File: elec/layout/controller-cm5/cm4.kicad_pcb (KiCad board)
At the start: 4 copper layers, 10 parts

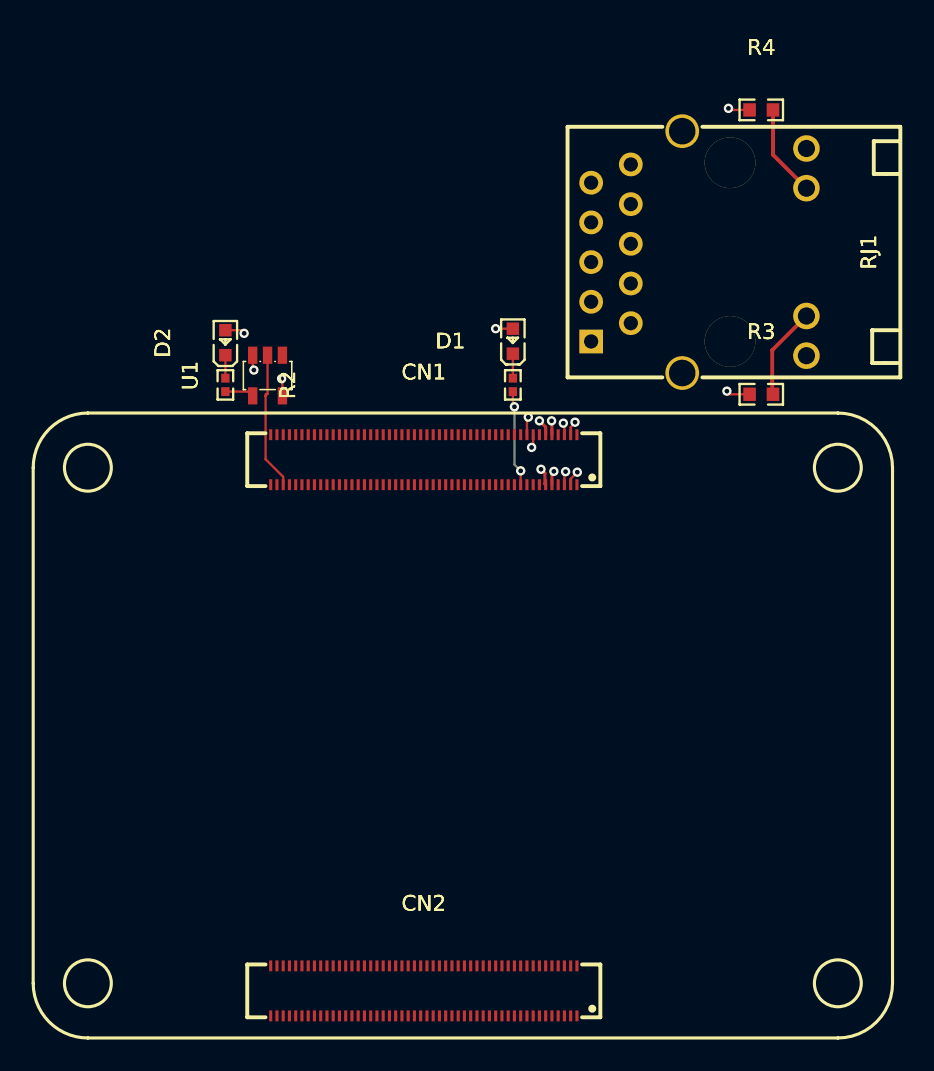
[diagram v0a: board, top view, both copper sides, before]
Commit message: re-sync layout + place mounting holes
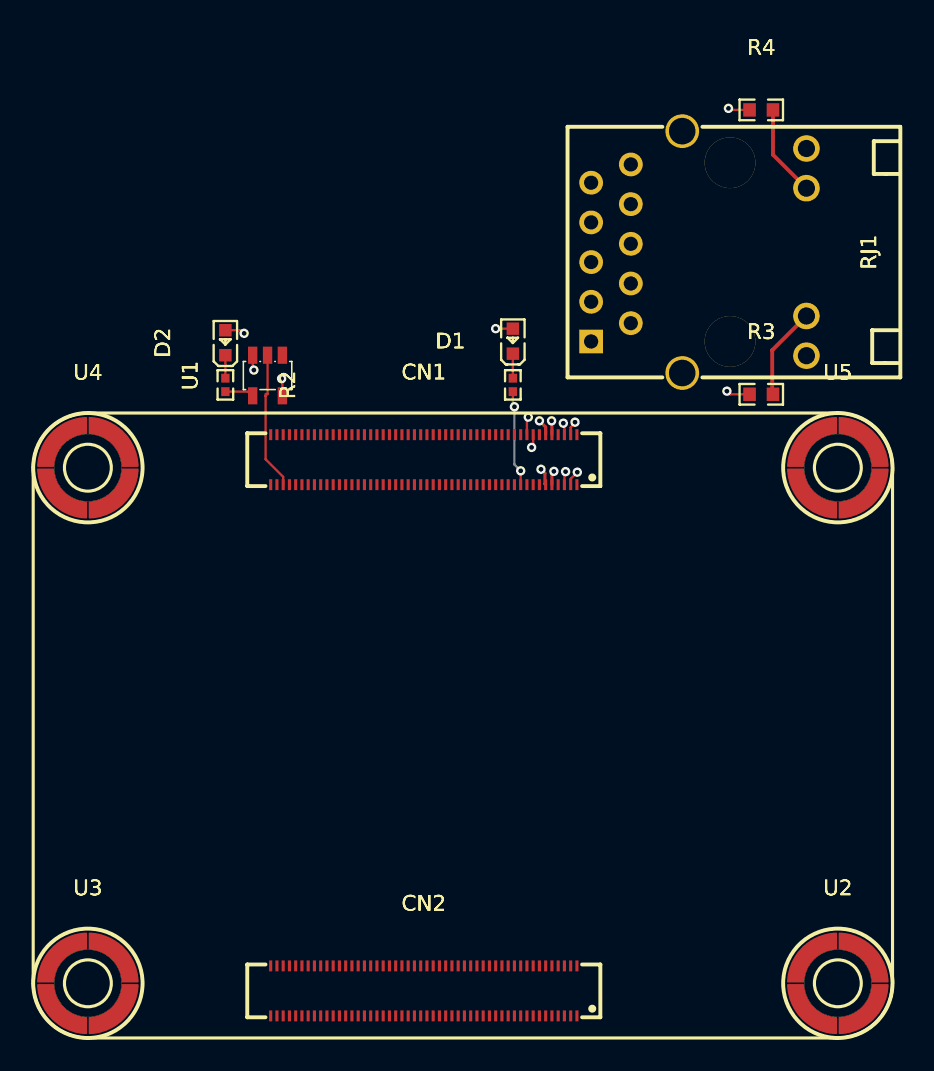
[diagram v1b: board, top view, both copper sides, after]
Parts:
- added U2: , atopile:SMD_BD5.6-D4.1-12eb58, F.Cu at (176.4, 136.8)
- added U3: , atopile:SMD_BD5.6-D4.1-12eb58, F.Cu at (128.4, 136.8)
- added U4: , atopile:SMD_BD5.6-D4.1-12eb58, F.Cu at (128.4, 103.8)
- added U5: , atopile:SMD_BD5.6-D4.1-12eb58, F.Cu at (176.4, 103.8)
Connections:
- net cm4-cathode renamed cm5-cathode
- net cm4-cathode-1 renamed cm5-cathode-1
- net cm4-line renamed cm5-line-3
- net cm4-line-1 renamed pins[57]
- net cm4-line-2 renamed cm5-line-7
- net cm4-line-3 renamed cm5-line-6
- net cm4-line-4 renamed pins[45]
- net cm4-line-5 renamed Y
- net cm4-line-6 renamed cm5-line-2
- net cm4-line-7 renamed cm5-line-1
- net cm4-pins[23] renamed cm5-line
- net cm4-pins[28] renamed cm5-line-10
- net cm4-pins[40] renamed cm5-pins[40]
- net cm4-pins[44] renamed cm5-pins[44]
- net cm4-pins[44]-1 renamed cm5-pins[44]-1
- net cm4-pins[98] renamed cm5-pins[98]
- net cm4-pins[99] renamed cm5-pins[99]
- net cm4.hdi_a-pins[15] renamed cm5.hdi_a-pins[15]
- net cm4.hdi_a-pins[17] renamed cm5.hdi_a-pins[17]
- net cm4.hdi_a-pins[34] renamed cm5.hdi_a-pins[34]
- net cm4.hdi_a-pins[35] renamed cm5.hdi_a-pins[35]
- net cm4.hdi_a-pins[56] renamed cm5.hdi_a-pins[56]
- net cm4.hdi_a-pins[62] renamed cm5.hdi_a-pins[62]
- net cm4.hdi_a-pins[68] renamed cm5.hdi_a-pins[68]
- net cm4.hdi_a-pins[74] renamed cm5.hdi_a-pins[74]
- net cm4.hdi_a-pins[88] renamed cm5.hdi_a-pins[88]
- net cm4.hdi_a-pins[92] renamed cm5.hdi_a-pins[92]
- net cm4.hdi_a-pins[93] renamed cm5.hdi_a-pins[93]
- net cm4.hdi_a-pins[94] renamed cm5.hdi_a-pins[94]
- net cm4.hdi_a-pins[98] renamed cm5.hdi_a-pins[98]
- net cm4.hdi_a-pins[99] renamed cm5.hdi_a-pins[99]
- net cm4.hdi_b-pins[15] renamed cm5.hdi_b-pins[15]
- net cm4.hdi_b-pins[17] renamed cm5.hdi_b-pins[17]
- net cm4.hdi_b-pins[23] renamed pins[23]
- net cm4.hdi_b-pins[28] renamed pins[28]
- net cm4.hdi_b-pins[34] renamed cm5.hdi_b-pins[34]
- net cm4.hdi_b-pins[35] renamed cm5-pins[35]
- net cm4.hdi_b-pins[40] renamed cm5.hdi_b-pins[40]
- net cm4.hdi_b-pins[56] renamed cm5-pins[56]
- net cm4.hdi_b-pins[62] renamed cm5-pins[62]
- net cm4.hdi_b-pins[68] renamed cm5-pins[68]
- net cm4.hdi_b-pins[74] renamed cm5.hdi_b-pins[74]
- net cm4.hdi_b-pins[88] renamed cm5.hdi_b-pins[88]
- net cm4.hdi_b-pins[92] renamed cm5.hdi_b-pins[92]
- net cm4.hdi_b-pins[93] renamed cm5.hdi_b-pins[93]
- net cm4.hdi_b-pins[94] renamed cm5.hdi_b-pins[94]
- net pins[30] renamed cm5-line-8
- net pins[43] renamed cm5-line-4
- net pins[47] renamed cm5-line-5
- net pins[50] renamed cm5-line-9
- CN1 pad 15: line -> line-1
- CN1 pad 17: line-1 -> line
- CN1 pad 27: line-2 -> line-3
- CN1 pad 82: line-3 -> line-2
- R3 pad 2: rj45-anode -> rj45-anode-1
- R4 pad 2: rj45-anode-1 -> rj45-anode
- RJ1 pad 12: rj45-anode -> rj45-anode-1
- RJ1 pad 13: rj45-anode-1 -> rj45-anode

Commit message: map i2c connections
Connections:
- net pins[49] renamed cm5.hdi_b-pins[49]
- CN1 pad 12: cm5-line -> cm5-line-2
- CN1 pad 15: line-1 -> line-2
- CN1 pad 17: line -> line-1
- CN1 pad 19: cm5-line-6 -> pins[37]
- CN1 pad 20: SCL -> cm5-line-9
- CN1 pad 24: cm5-line-5 -> cm5-line-8
- CN1 pad 25: cm5-line-2 -> cm5-pins[49]
- CN1 pad 28: cm5-line-3 -> SCL
- CN1 pad 29: pins[57] -> SDA
- CN1 pad 75: cm5-line-9 -> cm5-line-5
- CN1 pad 77: cm5-line-1 -> cm5-line
- CN1 pad 78: cm5-pins[44]-1 -> cm5-pins[44]
- CN1 pad 81: SDA -> cm5-line-6
- CN1 pad 82: line-2 -> line
- CN1 pad 85: cm5-line-8 -> cm5-line-1
- CN1 pad 86: cm5-line-10 -> cm5-line-3
- CN2 pad 78: cm5-pins[44] -> cm5-pins[44]-1
- D1 pad 1: cm5-cathode-1 -> cm5-cathode
- D2 pad 1: cm5-cathode -> cm5-cathode-1
- R1 pad 1: cm5-cathode-1 -> cm5-cathode
- R2 pad 1: cm5-cathode -> cm5-cathode-1
- R3 pad 2: rj45-anode-1 -> rj45-anode
- R4 pad 2: rj45-anode -> rj45-anode-1
- RJ1 pad 12: rj45-anode-1 -> rj45-anode
- RJ1 pad 13: rj45-anode -> rj45-anode-1
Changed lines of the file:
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@@
 	(net 0 "")
 	(net 1 "pins[20]")
-	(net 2 "cm5-pins[44]-1")
+	(net 2 "cm5-pins[44]")
 	(net 3 "cm5-pins[62]")
 	(net 4 "cm5.hdi_a-pins[74]")
 	(net 5 "cm5-line-4")
-	(net 6 "cm5-line-5")
+	(net 6 "cm5-line-8")
 	(net 7 "cm5.hdi_b-pins[74]")
 	(net 8 "cm5.hdi_a-pins[62]")
@@
 	(net 11 "pins[46]")
 	(net 12 "pins[67]")
-	(net 13 "cm5-line-10")
+	(net 13 "cm5-line-3")
 	(net 14 "UART_TX")
 	(net 15 "pins[5]")
 	(net 16 "VCC_5V")
 	(net 17 "UART_RX")
-	(net 18 "cm5-line-3")
+	(net 18 "SCL")
 	(net 19 "HDMI0_D1_N")
 	(net 20 "HDMI0_D2_N")
@@
 	(net 28 "pins[90]")
 	(net 29 "pins[82]")
-	(net 30 "line-1")
+	(net 30 "line-2")
 	(net 31 "pins[58]")
-	(net 32 "pins[57]")
+	(net 32 "SDA")
 	(net 33 "HDMI0_D0_P")
-	(net 34 "cm5-pins[44]")
+	(net 34 "cm5-pins[44]-1")
 	(net 35 "pins[76]")
 	(net 36 "cm5.hdi_a-pins[88]")
 	(net 37 "HDMI1_D2_P")
-	(net 38 "line-2")
+	(net 38 "line")
 	(net 39 "HDMI1_CK_N")
 	(net 40 "pins[79]")
@@
 	(net 46 "pins[33]")
 	(net 47 "pins[66]")
-	(net 48 "cm5-line-9")
+	(net 48 "cm5-line-5")
 	(net 49 "cm5.hdi_b-pins[88]")
 	(net 50 "cm5.hdi_b-pins[92]")
-	(net 51 "cm5-line-6")
-	(net 52 "cm5-line")
+	(net 51 "pins[37]")
+	(net 52 "cm5-line-2")
 	(net 53 "pins[29]")
-	(net 54 "pins[49]")
+	(net 54 "cm5.hdi_b-pins[49]")
 	(net 55 "HDMI1_D0_N")
 	(net 56 "cm5-pins[35]")
@@
 	(net 67 "rj45.connector-net-1")
 	(net 68 "Y")
-	(net 69 "cm5-cathode-1")
-	(net 70 "cm5-cathode")
-	(net 71 "rj45-anode")
+	(net 69 "cm5-cathode")
+	(net 70 "cm5-cathode-1")
+	(net 71 "rj45-anode-1")
 	(net 72 "rj45.connector-net")
 	(net 73 "N_C_")
-	(net 74 "rj45-anode-1")
+	(net 74 "rj45-anode")
 	(net 75 "pins[45]")
 	(net 76 "pins[3]")
@@
 	(net 82 "pins[41]")
 	(net 83 "pins[70]")
-	(net 84 "cm5-line-2")
+	(net 84 "cm5-pins[49]")
 	(net 85 "cm5.hdi_a-pins[98]")
 	(net 86 "cm5.hdi_b-pins[34]")
@@
 	(net 92 "cm5.hdi_b-pins[40]")
 	(net 93 "pins[91]")
-	(net 94 "SCL")
+	(net 94 "cm5-line-9")
 	(net 95 "pins[64]")
 	(net 96 "pins[9]")
@@
 	(net 115 "pins[72]")
 	(net 116 "HDMI0_CK_N")
-	(net 117 "cm5-line-8")
+	(net 117 "cm5-line-1")
 	(net 118 "HDMI0_D2_P")
 	(net 119 "pins[22]")
-	(net 120 "line")
+	(net 120 "line-1")
 	(net 121 "pins[80]")
 	(net 122 "cm5.hdi_b-pins[94]")
@@
 	(net 124 "pins[96]")
 	(net 125 "pins[14]")
-	(net 126 "cm5-line-1")
+	(net 126 "cm5-line")
 	(net 127 "cm5.hdi_a-pins[94]")
 	(net 128 "cm5.hdi_a-pins[34]")
@@
 	(net 135 "pins[32]")
 	(net 136 "cm5.hdi_b-pins[93]")
-	(net 137 "SDA")
+	(net 137 "cm5-line-6")
 	(net 138 "cm5-pins[98]")
 	(net 139 "ETH_P0_P")
@@
 			)
 			(remove_unused_layers no)
-			(net 74 "rj45-anode-1")
+			(net 74 "rj45-anode")
 		)
 		(pad "13" thru_hole circle
@@
 			)
 			(remove_unused_layers no)
-			(net 71 "rj45-anode")
+			(net 71 "rj45-anode-1")
 		)
 		(pad "14" thru_hole circle
@@
 			(size 0.8 0.8)
 			(layers "F.Cu" "F.Paste" "F.Mask")
-			(net 70 "cm5-cathode")
+			(net 70 "cm5-cathode-1")
 		)
 		(pad "2" smd rect
@@
 			(size 0.57 0.54)
 			(layers "F.Cu" "F.Paste" "F.Mask")
-			(net 70 "cm5-cathode")
+			(net 70 "cm5-cathode-1")
 		)
 		(pad "2" smd rect
@@
 			(size 0.8 0.8)
 			(layers "F.Cu" "F.Paste" "F.Mask")
-			(net 69 "cm5-cathode-1")
+			(net 69 "cm5-cathode")
 		)
 		(pad "2" smd rect
@@
 			(size 0.81 0.86)
 			(layers "F.Cu" "F.Paste" "F.Mask")
-			(net 71 "rj45-anode")
+			(net 71 "rj45-anode-1")
 		)
 	)
@@
 			(size 0.2 0.7)
 			(layers "F.Cu" "F.Paste" "F.Mask")
-			(net 54 "pins[49]")
+			(net 54 "cm5.hdi_b-pins[49]")
 		)
 		(pad "26" smd rect
@@
 			(size 0.2 0.7)
 			(layers "F.Cu" "F.Paste" "F.Mask")
-			(net 34 "cm5-pins[44]")
+			(net 34 "cm5-pins[44]-1")
 		)
 		(pad "79" smd rect
@@
 			(size 0.81 0.86)
 			(layers "F.Cu" "F.Paste" "F.Mask")
-			(net 74 "rj45-anode-1")
+			(net 74 "rj45-anode")
 		)
 	)
@@
 			(size 0.57 0.54)
 			(layers "F.Cu" "F.Paste" "F.Mask")
-			(net 69 "cm5-cathode-1")
+			(net 69 "cm5-cathode")
 		)
 		(pad "2" smd rect
@@
 			(size 0.2 0.7)
 			(layers "F.Cu" "F.Paste" "F.Mask")
-			(net 52 "cm5-line")
+			(net 52 "cm5-line-2")
 		)
 		(pad "13" smd rect
@@
 			(size 0.2 0.7)
 			(layers "F.Cu" "F.Paste" "F.Mask")
-			(net 30 "line-1")
+			(net 30 "line-2")
 		)
 		(pad "16" smd rect
@@
 			(size 0.2 0.7)
 			(layers "F.Cu" "F.Paste" "F.Mask")
-			(net 120 "line")
+			(net 120 "line-1")
 		)
 		(pad "18" smd rect
@@
 			(size 0.2 0.7)
 			(layers "F.Cu" "F.Paste" "F.Mask")
-			(net 51 "cm5-line-6")
+			(net 51 "pins[37]")
 		)
 		(pad "20" smd rect
@@
 			(size 0.2 0.7)
 			(layers "F.Cu" "F.Paste" "F.Mask")
-			(net 94 "SCL")
+			(net 94 "cm5-line-9")
 		)
 		(pad "21" smd rect
@@
 			(size 0.2 0.7)
 			(layers "F.Cu" "F.Paste" "F.Mask")
-			(net 6 "cm5-line-5")
+			(net 6 "cm5-line-8")
 		)
 		(pad "25" smd rect
@@
 			(size 0.2 0.7)
 			(layers "F.Cu" "F.Paste" "F.Mask")
-			(net 84 "cm5-line-2")
+			(net 84 "cm5-pins[49]")
 		)
 		(pad "26" smd rect
@@
 			(size 0.2 0.7)
 			(layers "F.Cu" "F.Paste" "F.Mask")
-			(net 18 "cm5-line-3")
+			(net 18 "SCL")
 		)
 		(pad "29" smd rect
@@
 			(size 0.2 0.7)
 			(layers "F.Cu" "F.Paste" "F.Mask")
-			(net 32 "pins[57]")
+			(net 32 "SDA")
 		)
 		(pad "30" smd rect
@@
 			(size 0.2 0.7)
 			(layers "F.Cu" "F.Paste" "F.Mask")
-			(net 48 "cm5-line-9")
+			(net 48 "cm5-line-5")
 		)
 		(pad "76" smd rect
@@
 			(size 0.2 0.7)
 			(layers "F.Cu" "F.Paste" "F.Mask")
-			(net 126 "cm5-line-1")
+			(net 126 "cm5-line")
 		)
 		(pad "78" smd rect
@@
 			(size 0.2 0.7)
 			(layers "F.Cu" "F.Paste" "F.Mask")
-			(net 2 "cm5-pins[44]-1")
+			(net 2 "cm5-pins[44]")
 		)
 		(pad "79" smd rect
@@
 			(size 0.2 0.7)
 			(layers "F.Cu" "F.Paste" "F.Mask")
-			(net 137 "SDA")
+			(net 137 "cm5-line-6")
 		)
 		(pad "82" smd rect
@@
 			(size 0.2 0.7)
 			(layers "F.Cu" "F.Paste" "F.Mask")
-			(net 38 "line-2")
+			(net 38 "line")
 		)
 		(pad "83" smd rect
@@
 			(size 0.2 0.7)
 			(layers "F.Cu" "F.Paste" "F.Mask")
-			(net 117 "cm5-line-8")
+			(net 117 "cm5-line-1")
 		)
 		(pad "86" smd rect
@@
 			(size 0.2 0.7)
 			(layers "F.Cu" "F.Paste" "F.Mask")
-			(net 13 "cm5-line-10")
+			(net 13 "cm5-line-3")
 		)
 		(pad "87" smd rect

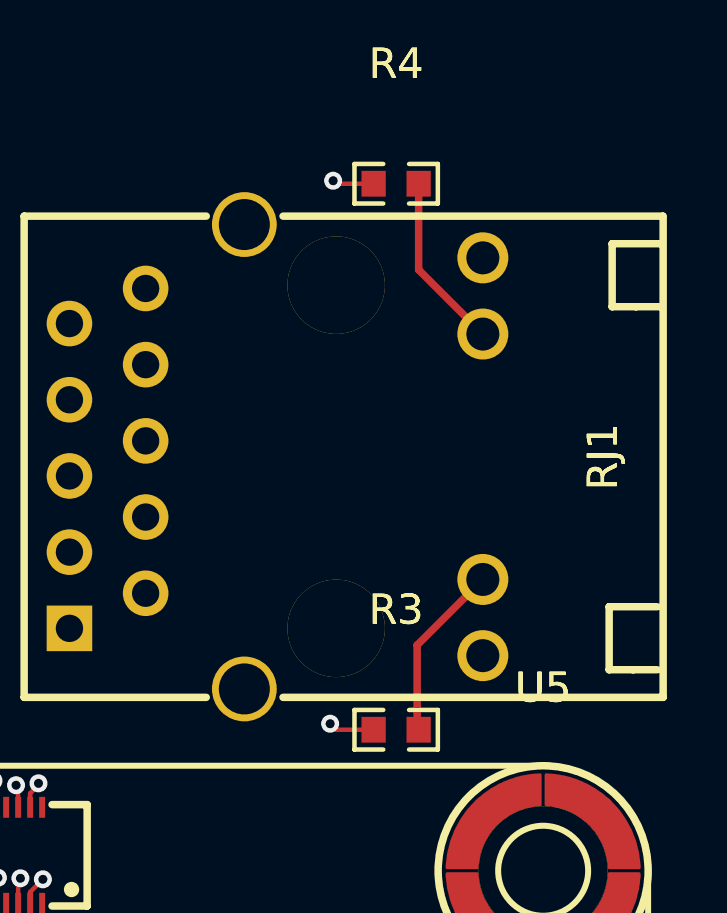
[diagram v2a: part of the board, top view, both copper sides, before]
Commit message: fix link light led polarity
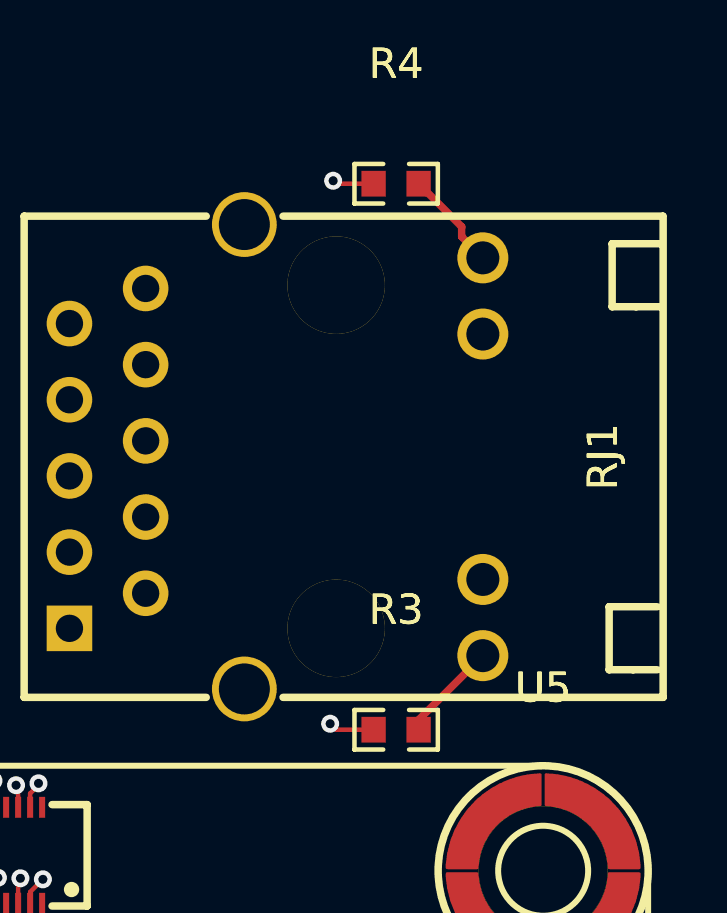
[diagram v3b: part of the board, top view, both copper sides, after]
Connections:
- net cm5-line-9 renamed line-6
- net cm5-pins[44]-1 renamed pins[44]
- net cm5.hdi_b-pins[40] renamed pins[40]
- net cm5.hdi_b-pins[49] renamed pins[49]
- net pins[26] renamed cm5.hdi_b-pins[26]
- net pins[46] renamed cm5-pins[46]
- net pins[79] renamed line-7
- CN1 pad 12: cm5-line-2 -> cm5-line-4
- CN1 pad 15: line-2 -> line-4
- CN1 pad 17: line-1 -> line-2
- CN1 pad 19: pins[37] -> cm5-line-6
- CN1 pad 22: cm5-line-4 -> pins[43]
- CN1 pad 23: pins[45] -> cm5-line-7
- CN1 pad 24: cm5-line-8 -> pins[47]
- CN1 pad 25: cm5-pins[49] -> cm5-line-8
- CN1 pad 27: line-3 -> line-1
- CN1 pad 41: pins[81] -> line
- CN1 pad 75: cm5-line-5 -> pins[50]
- CN1 pad 77: cm5-line -> cm5-pins[46]-1
- CN1 pad 78: cm5-pins[44] -> cm5-line-1
- CN1 pad 80: cm5-pins[40] -> cm5-line-5
- CN1 pad 81: cm5-line-6 -> line-3
- CN1 pad 82: line -> line-5
- CN1 pad 85: cm5-line-1 -> cm5-line-2
- CN1 pad 87: cm5-line-7 -> cm5-pins[26]
- D1 pad 1: cm5-cathode -> cm5-cathode-1
- D2 pad 1: cm5-cathode-1 -> cm5-cathode
- R1 pad 1: cm5-cathode -> cm5-cathode-1
- R2 pad 1: cm5-cathode-1 -> cm5-cathode
- R2 pad 2: Y -> cm5-line
- R3 pad 2: rj45-anode -> rj45-anode-1
- R4 pad 2: rj45-anode-1 -> rj45-anode
- RJ1 pad 11: ETH_LED_LINK -> rj45-anode-1
- RJ1 pad 12: rj45-anode -> ETH_LED_LINK
- RJ1 pad 13: rj45-anode-1 -> ETH_LED_ACTIVITY
- RJ1 pad 14: ETH_LED_ACTIVITY -> rj45-anode
- U1 pad 4: Y -> cm5-line
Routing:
- net rj45-anode: track 5.94 -> 3.36 mm
- net rj45-anode-1: track 5.90 -> 3.36 mm
- net cm5-line: track 0.00 -> 1.86 mm
- net Y: track 1.86 -> 0.00 mm
- net ETH_LED_LINK: track 23.5 -> 24.6 mm
- net ETH_LED_ACTIVITY: track 30.6 -> 29.5 mm
